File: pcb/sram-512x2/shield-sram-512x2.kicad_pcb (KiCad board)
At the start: 4 copper layers, 100 x 100 mm, 19 parts, among them J1 QSH-060-01-L-D-A, J2 QSH-060-01-L-D-A, U1 IS61WV25616-10TLI, U2 IS61WV25616-10TLI

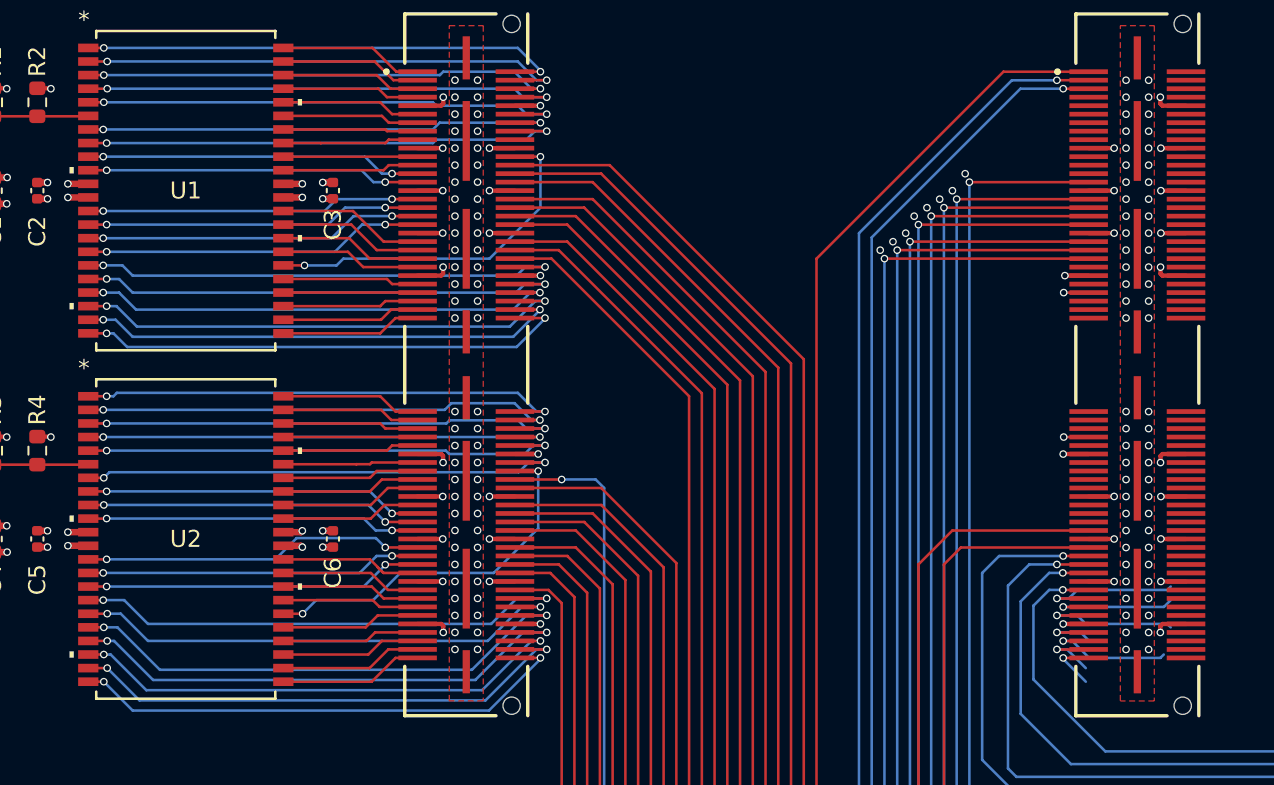
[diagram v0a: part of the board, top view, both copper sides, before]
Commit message: [sram][scripts][pins] update 512 sram to avoid pll pin
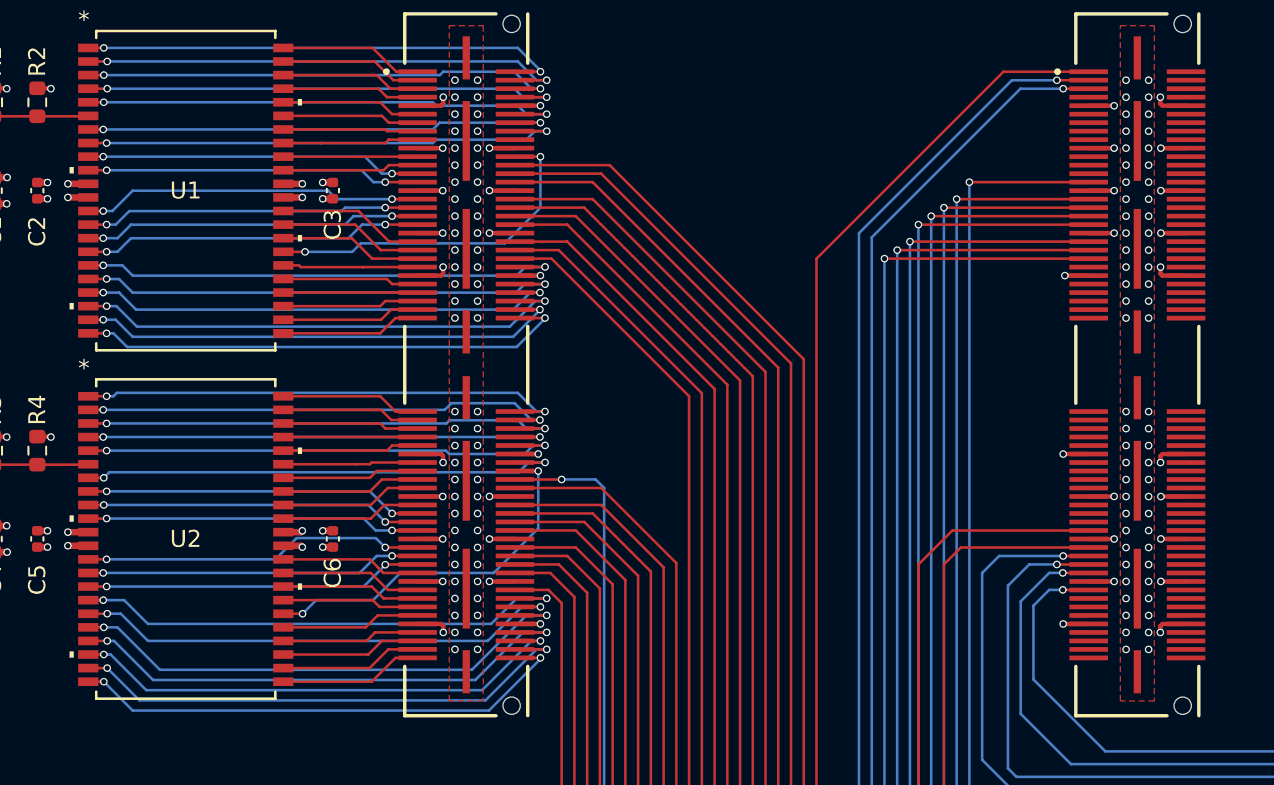
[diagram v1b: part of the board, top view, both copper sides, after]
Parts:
- U1, U2: value IS61WV25616-10TLI -> IS61WV51216-10TLI
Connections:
- U1 pad 28: A18 -> A39
- U1 pad 29: A39 -> A18
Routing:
- net D41: track 8.86 -> 0.00 mm, vias 1 -> 0
- net D37: track 8.86 -> 0.00 mm, vias 1 -> 0
- net D39: track 8.03 -> 0.00 mm, vias 1 -> 0
- net D45: track 7.92 -> 0.00 mm, vias 1 -> 0
- net D47: track 4.03 -> 0.00 mm, vias 1 -> 0
- net D43: track 3.98 -> 0.00 mm, vias 1 -> 0
- net D49: track 3.45 -> 0.00 mm, vias 1 -> 0
- net +3V3: track 75.4 -> 76.9 mm, vias 56 -> 57
- net D7: track 1.47 -> 0.00 mm, vias 1 -> 0
- net C43: track 1.47 -> 0.00 mm, vias 1 -> 0
- net GND: vias 344 -> 336
